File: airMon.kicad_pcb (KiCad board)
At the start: 2 copper layers, 64.8 x 99.7 mm, 120 parts, among them J1 JTAG, J10 I2C_2_2, J11 I2C_2_3_Buffer, J12 I2C_2_4_Buffer, J13 GPS, J14 A3, J15 A4, J16 Rain, J17 GPIO, J18 Wind, J19 USB_B_Micro, J2 PMS7003, J20 Power, J3 PMSx003, J4 SDS011, J5 Conn_01x05, J6 SW, J7 I2C_1_1, J8 I2C_1_2, J9 I2C_2_1, Q1 2N7002NXAK, Q2 BSH202, Q3 SS8050, Q4 SS8050, Q5 2N7002NXAK, Q6 BSH202, Q7 2N7002NXAK, Q8 BSH202, U1 ESP32-WROOM-32, U2 P82B715, U3 L70/L76/MAX-M8C/MAX-M8Q/MAX-8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, U4 PCA9536D, U5 CH340C, U6 LMR14010ADDCR, U7 LMR14010ADDCR

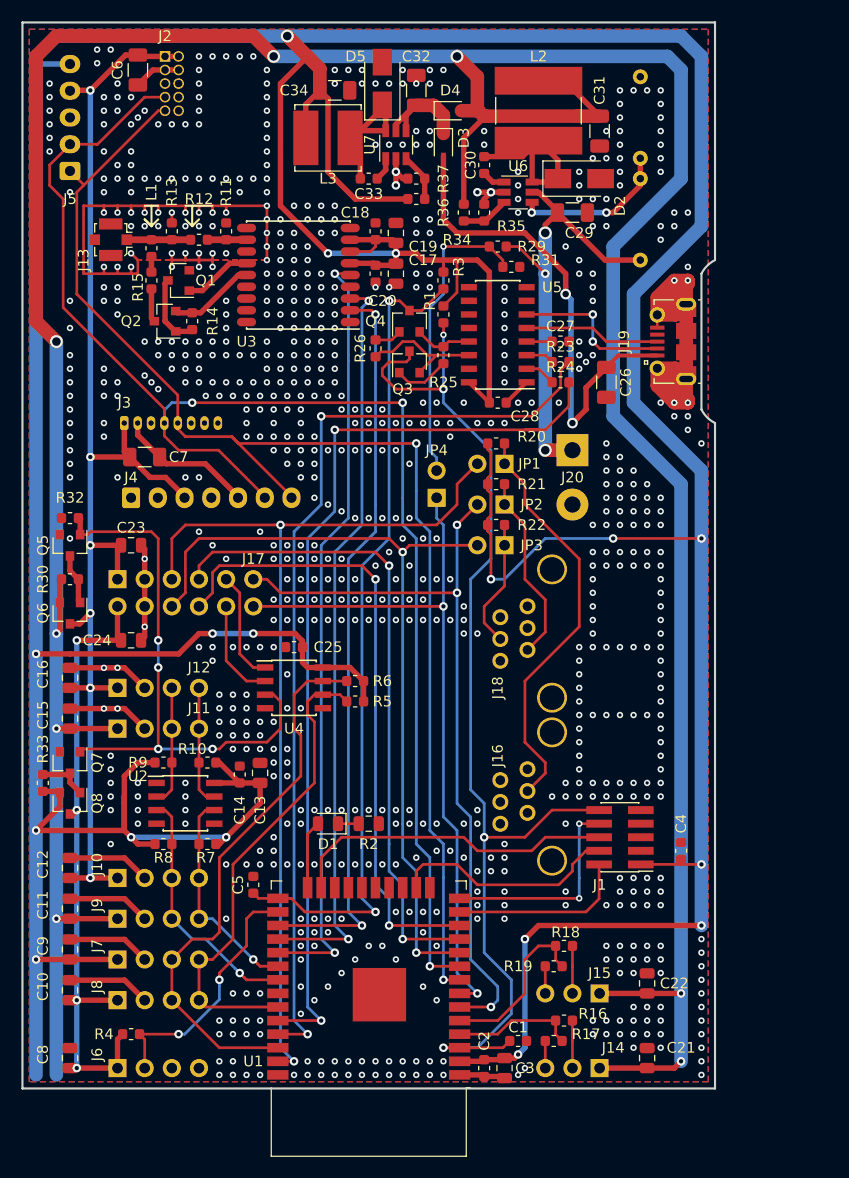
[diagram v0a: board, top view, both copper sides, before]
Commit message: Added reverse polarity protection Improved power switch mosfets
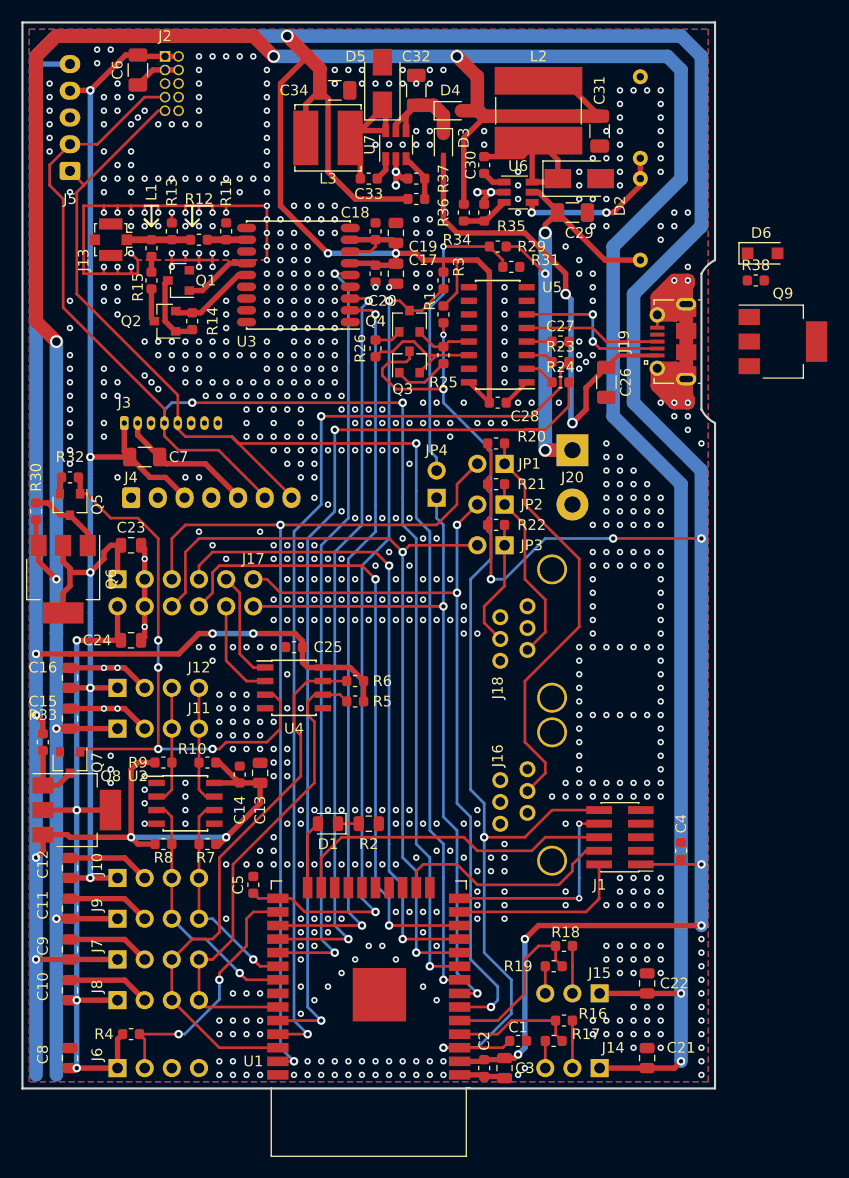
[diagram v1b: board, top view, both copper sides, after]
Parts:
- added D6: KDZVTR8.2B, Diode_SMD:D_SOD-123F, F.Cu at (88.3, 40.6)
- added Q9: DMP6023LE-13, Package_TO_SOT_SMD:SOT-223-3_TabPin2, F.Cu at (90.2, 48.9)
- added R38: 47k, Resistor_SMD:R_0603_1608Metric, F.Cu at (87.6, 43.2)
- Q6, Q8: value BSH202 -> DMP6023LE-13; footprint Package_TO_SOT_SMD:SOT-23 -> Package_TO_SOT_SMD:SOT-223-3_TabPin2
- moved R30 7.10 mm to (20.3, 64.8), turned to 90 degrees
- moved R32 3.81 mm to (23.5, 61.6)
- moved R33 3.81 mm to (21.0, 86.4), turned to 270 degrees
- moved Q5 3.81 mm to (23.5, 64.1)
- moved Q6 3.24 mm to (22.9, 71.1)
- moved Q8 0.90 mm to (24.1, 92.7), turned to 0 degrees
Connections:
- J20 pad 1: +VDC -> Net-(J20-Pad1)
- Q6 pad 2: +5V -> 5V_Switched
- Q6 pad 3: 5V_Switched -> +5V
- Q8 pad 2: VCC -> 3.3V_Switched
- Q8 pad 3: 3.3V_Switched -> VCC
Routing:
- net 5V_Switched: track 116.6 -> 124.4 mm, vias 6 -> 5
- net 3.3V_Switched: track 60.5 -> 66.0 mm
- net VCC: track 520.3 -> 515.0 mm, vias 17 -> 18
- net Net-(Q5-Pad3): track 4.74 -> 7.18 mm
- net Net-(Q7-Pad3): track 4.79 -> 6.43 mm
- net VSS: track 184.3 -> 185.9 mm, vias 780 -> 775
- net +5V: track 334.5 -> 335.6 mm
- net /POWER: track 53.2 -> 54.2 mm

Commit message: Added reverse polarity protection Changed power switch MOSFETs to a lower RDS(on) model Improved buck converter layout Improved USB layout
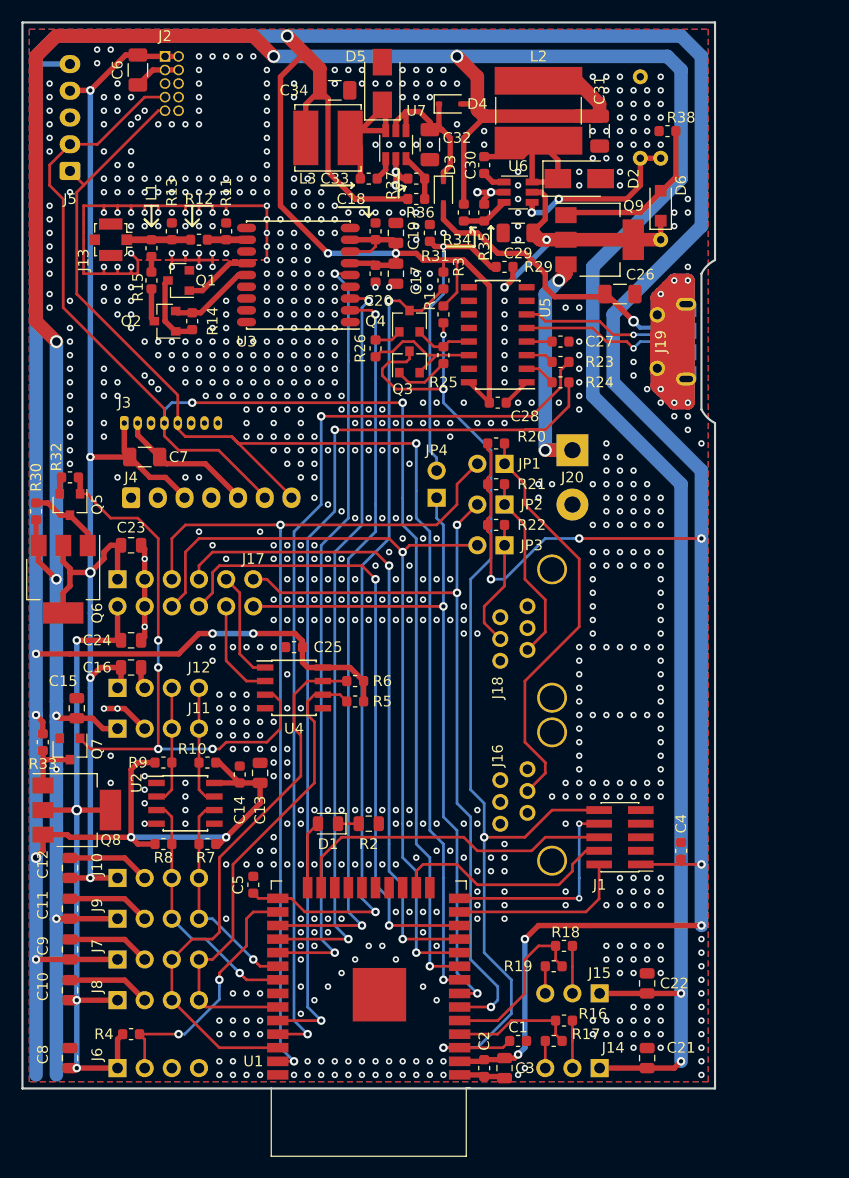
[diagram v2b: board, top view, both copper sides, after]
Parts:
- J19: moved to B.Cu
- R30, R33: value 10k -> 100k
- R38: value 47k -> 1M
- moved Q9 19.6 mm to (73.0, 39.4)
- moved R38 16.2 mm to (79.4, 29.2), turned to 180 degrees
- moved D6 10.5 mm to (78.7, 36.2), turned to 90 degrees
- moved C26 8.35 mm to (74.9, 44.5), turned to 0 degrees
- moved R31 8.25 mm to (57.1, 38.7), turned to 90 degrees
- moved C16 5.80 mm to (29.2, 79.4), turned to 0 degrees
- moved C29 5.43 mm to (65.4, 38.7), turned to 180 degrees
- moved C32 5.24 mm to (57.1, 30.5), turned to 270 degrees
- moved D3 4.44 mm to (58.4, 34.9)
- moved R27 2.69 mm to (78.7, 39.4)
- moved R29 2.01 mm to (64.1, 41.9)
- moved Q7 1.27 mm to (23.5, 87.0)
- moved C15 1.16 mm to (24.1, 83.2)
- moved D4 0.63 mm to (59.1, 26.7)
- turned J19 to 270 degrees
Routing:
- net VSS: track 185.9 -> 281.0 mm, vias 775 -> 831
- net Net-(J20-Pad1): track 0.00 -> 23.3 mm, vias 0 -> 2
- net VBUS: track 45.4 -> 26.6 mm, vias 2 -> 1
- net +VDC: track 45.3 -> 27.6 mm, vias 3 -> 2
- net Net-(D6-Pad2): track 0.00 -> 16.1 mm
- net Net-(C32-Pad1): track 10.6 -> 16.4 mm
- net +5V: track 335.6 -> 340.7 mm, vias 8 -> 9
- net Net-(J19-Pad2): track 15.0 -> 13.0 mm, vias 2 -> 1
- net Net-(R27-Pad2): track 14.7 -> 16.6 mm
- net VCC: track 515.0 -> 516.2 mm
- net 5V_Switched: track 124.4 -> 125.3 mm
- net Net-(Q7-Pad3): track 6.43 -> 5.90 mm
- net Net-(J19-Pad3): track 12.7 -> 13.3 mm, vias 0 -> 1

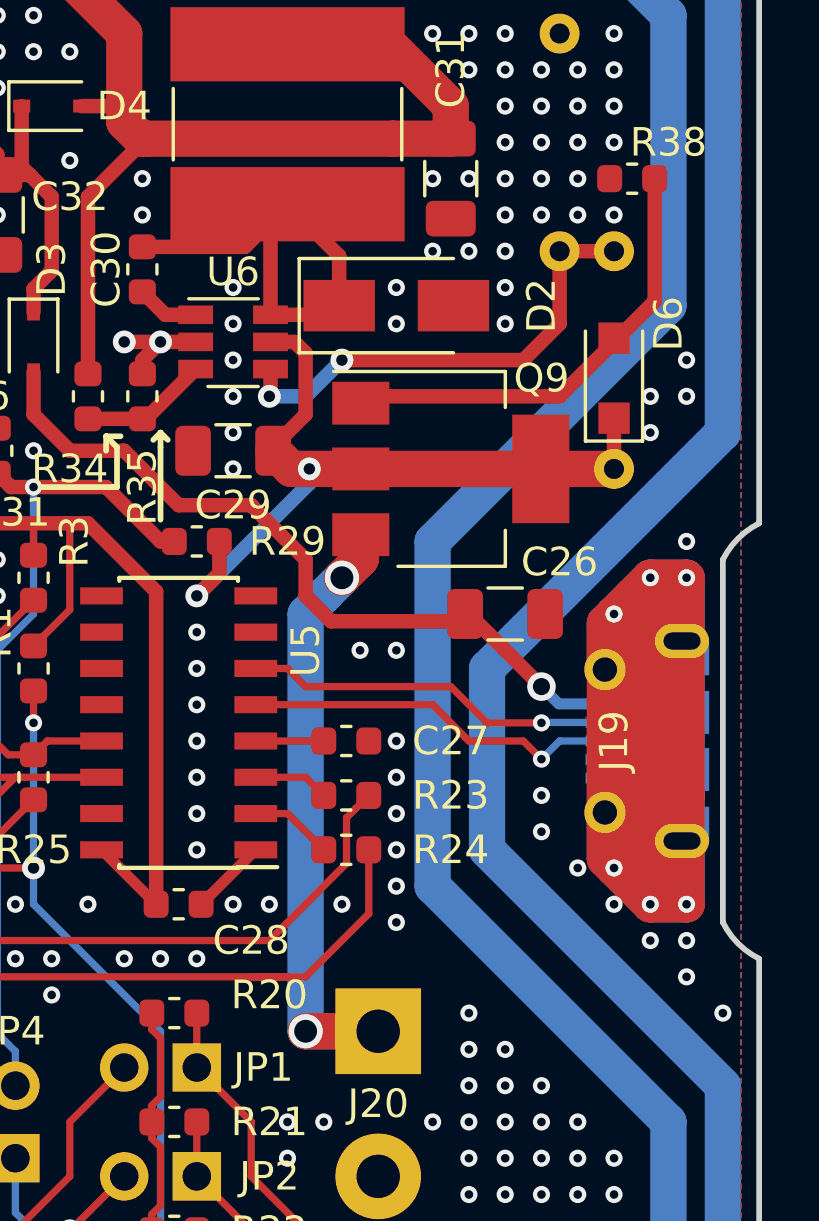
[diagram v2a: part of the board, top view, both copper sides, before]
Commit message: Fixed reverse polarity protection
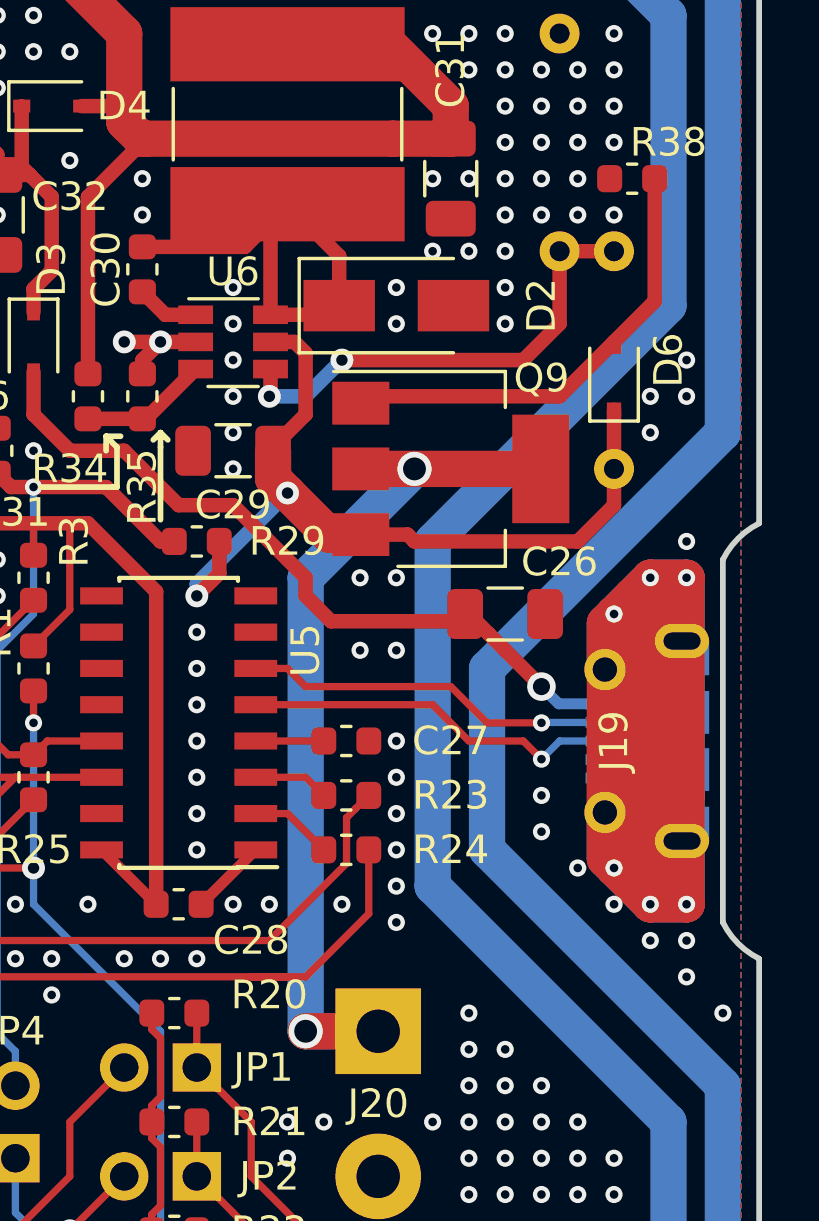
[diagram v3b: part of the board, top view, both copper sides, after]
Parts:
- D6: value KDZVTR8.2B -> UDZVTE-1712B; footprint Diode_SMD:D_SOD-123F -> Diode_SMD:D_SOD-323F
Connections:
- Q9 pad 2: +VDC -> Net-(J20-Pad1)
- Q9 pad 3: Net-(J20-Pad1) -> +VDC
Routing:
- net Net-(J20-Pad1): track 23.3 -> 32.6 mm
- net +VDC: track 27.6 -> 30.1 mm
- net VSS: vias 831 -> 833

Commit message: Added fuse for USB Added buttons for boot and reset Added version number to PCB Changed several component values for improved manufacturing Added BOM Added component position file
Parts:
- added F1: Polyfuse, Fuse:Fuse_0603_1608Metric, F.Cu at (70.5, 44.5)
- added SW1: RESET, Button_Switch_SMD:SW_SPST_SKQG_WithStem, F.Cu at (54.6, 88.3)
- added SW2: Boot, Button_Switch_SMD:SW_SPST_SKQG_WithStem, F.Cu at (48.3, 88.3)
- Q1, Q5, Q7: value 2N7002NXAK -> 2N7002
- Q2: value BSH202 -> AO3401A
- R27: value 111k -> DNP
- R28: value 29k1 -> DNP
- R29, R36: value 64k9 -> 110k
- R31: value 4k7 -> 10k
- R32: value 10k -> 100k
- R34: value 111k -> 110k
- R37: value 19k6 -> 33k
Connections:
- C26 pad 1: VBUS -> Net-(C26-Pad1)
- J19 pad 1: VBUS -> Net-(C26-Pad1)
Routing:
- net VCC: track 516.2 -> 505.0 mm
- net /EN: track 105.3 -> 116.0 mm, vias 4 -> 5
- net VBUS: track 26.3 -> 15.7 mm, vias 1 -> 0
- net /Boot: track 77.2 -> 87.8 mm, vias 2 -> 3
- net Net-(C26-Pad1): track 0.00 -> 8.81 mm, vias 0 -> 1
- net /POWER: track 54.6 -> 51.0 mm
- net /SDA_1: track 45.2 -> 44.7 mm
- net /SCL_1: track 52.2 -> 51.6 mm
- net VSS: vias 833 -> 851
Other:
- board text added: "BOOT"
- board text added: "JLCJLCJLCJLC"
- board text added: "RESET"
- board text added: "v0.1"

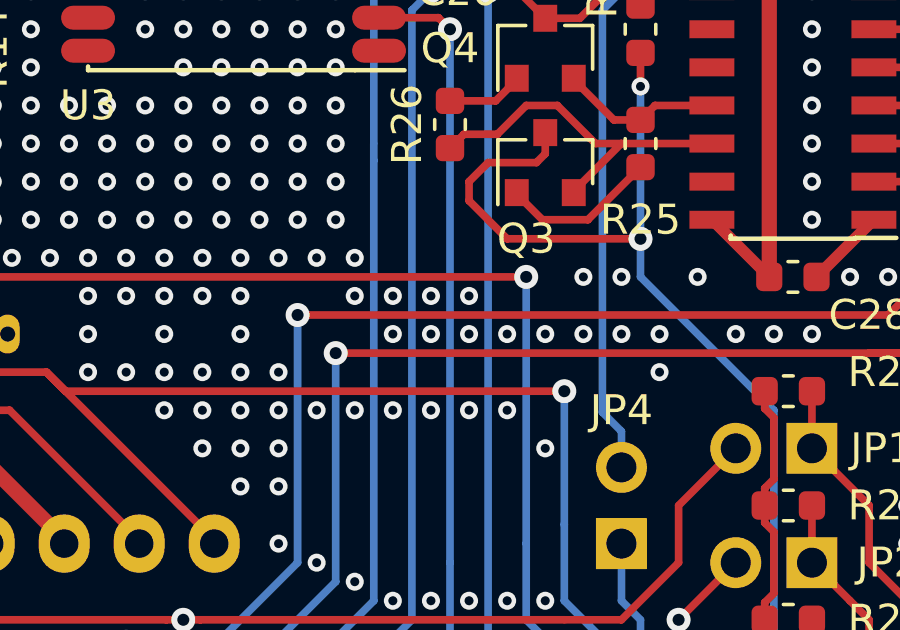
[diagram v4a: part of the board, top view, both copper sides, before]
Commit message: Moved to KiCad 5.1.5_3
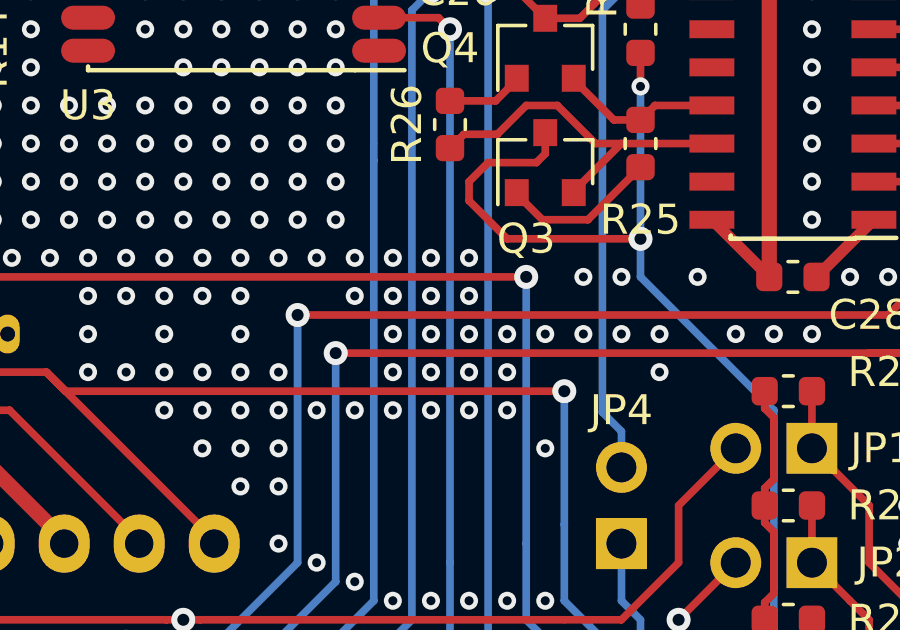
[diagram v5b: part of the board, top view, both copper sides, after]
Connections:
- U1 pad 39: (no net) -> VSS
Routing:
- net VSS: vias 851 -> 858
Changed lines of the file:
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@@
-(kicad_pcb (version 20171130) (host pcbnew "(5.0.2)-1")
+(kicad_pcb (version 20171130) (host pcbnew "(5.1.5)-3")
   (general
     (thickness 1.6)
     (drawings 97)
-    (tracks 1881)
+    (tracks 1888)
     (zones 0)
     (modules 126)
@@
     (zone_45_only no)
     (trace_min 0.127)
-    (segment_width 0.2)
-    (edge_width 0.2)
     (via_size 0.8)
     (via_drill 0.4)
@@
     (uvia_min_size 0.2)
     (uvia_min_drill 0.1)
+    (edge_width 0.2)
+    (segment_width 0.2)
     (pcb_text_width 0.3)
     (pcb_text_size 1.5 1.5)
@@
   (module global:PMS7003 (layer B.Cu)
     (at 51.0032 35.2552 180)
-    (fp_text reference REF** (at 0 -1 180) (layer B.SilkS) hide
+    (fp_text reference REF** (at 0 -1) (layer B.SilkS) hide
       (effects (font (size 1 1) (thickness 0.15)) (justify mirror))
     )
-    (fp_text value PMS7003 (at 0 1 180) (layer B.Fab) hide
+    (fp_text value PMS7003 (at 0 1) (layer B.Fab) hide
       (effects (font (size 1 1) (thickness 0.15)) (justify mirror))
     )
-    (fp_text user 9 (at 19.27 7.96 180) (layer B.Fab)
+    (fp_text user 9 (at 19.27 7.96) (layer B.Fab)
       (effects (font (size 1 1) (thickness 0.15)) (justify mirror))
     )
-    (fp_text user 10 (at 16.095 7.96 180) (layer B.Fab)
+    (fp_text user 10 (at 16.095 7.96) (layer B.Fab)
       (effects (font (size 1 1) (thickness 0.15)) (justify mirror))
     )
-    (fp_text user 2 (at 16.73 13.04 180) (layer B.Fab)
+    (fp_text user 2 (at 16.73 13.04) (layer B.Fab)
       (effects (font (size 1 1) (thickness 0.15)) (justify mirror))
     )
-    (fp_text user 1 (at 19.27 13.04 180) (layer B.Fab)
+    (fp_text user 1 (at 19.27 13.04) (layer B.Fab)
       (effects (font (size 1 1) (thickness 0.15)) (justify mirror))
     )
@@
     (fp_line (start 21 15.5) (end 15 15.5) (layer B.SilkS) (width 0.12))
     (fp_line (start 21 15.5) (end 21 5.5) (layer B.SilkS) (width 0.12))
-    (fp_line (start 23.95 18.45) (end -23.95 18.45) (layer B.CrtYd) (width 0.12))
-    (fp_line (start 23.95 -18.45) (end 23.95 18.45) (layer B.CrtYd) (width 0.12))
-    (fp_line (start -23.95 -18.45) (end 23.95 -18.45) (layer B.CrtYd) (width 0.12))
-    (fp_line (start -23.95 18.45) (end -23.95 -18.45) (layer B.CrtYd) (width 0.12))
     (fp_line (start 23.85 -18.35) (end 23.85 18.35) (layer B.SilkS) (width 0.12))
     (fp_line (start -23.85 -18.35) (end -23.85 18.35) (layer B.SilkS) (width 0.12))
@@
     (fp_line (start -9.12 -15.865) (end -9.12 -9.445) (layer F.SilkS) (width 0.12))
     (fp_line (start -9.12 -9.445) (end -9.5 -9.445) (layer F.SilkS) (width 0.12))
-    (pad 39 smd rect (at -1 -0.755 180) (size 5 5) (layers F.Cu F.Paste F.Mask))
+    (pad 39 smd rect (at -1 -0.755 180) (size 5 5) (layers F.Cu F.Paste F.Mask)
+      (net 1 VSS))
     (pad 1 smd rect (at -8.5 -8.255 180) (size 2 0.9) (layers F.Cu F.Paste F.Mask)
       (net 1 VSS))
@@
   (via (at 20.32 109.855) (size 0.6) (drill 0.3) (layers F.Cu B.Cu) (net 1))
   (via (at 20.32 108.585) (size 0.6) (drill 0.3) (layers F.Cu B.Cu) (net 1))
+  (via (at 50.165 57.785) (size 0.6) (drill 0.3) (layers F.Cu B.Cu) (net 1))
+  (via (at 53.975 57.785) (size 0.6) (drill 0.3) (layers F.Cu B.Cu) (net 1))
+  (via (at 52.705 57.785) (size 0.6) (drill 0.3) (layers F.Cu B.Cu) (net 1))
+  (via (at 51.435 57.785) (size 0.6) (drill 0.3) (layers F.Cu B.Cu) (net 1))
+  (via (at 52.705 53.975) (size 0.6) (drill 0.3) (layers F.Cu B.Cu) (net 1))
+  (via (at 51.435 53.975) (size 0.6) (drill 0.3) (layers F.Cu B.Cu) (net 1))
+  (via (at 50.165 53.975) (size 0.6) (drill 0.3) (layers F.Cu B.Cu) (net 1))
   (via (at 58.42 114.935) (size 0.8) (drill 0.4) (layers F.Cu B.Cu) (net 2))
   (segment (start 59.935 114.935) (end 58.42 114.935) (width 0.256) (layer F.Cu) (net 2))
